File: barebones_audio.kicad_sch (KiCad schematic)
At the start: 40 parts, among them U10 ES8316, U30 TS3A227EYFFR, U31 STM32H743VIH6, U38 TPA2012D2RTJT

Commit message: Fixed version control merge issues
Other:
- note added: "ADC + DAC"
- note removed: "AUTOMATIC AUDIO DET"
- note removed: "Error: Cannot add L1 (footprint 'XAL7030-472MEB:IND_XAL7030-472MEB' not found). Error: Cannot update L2 (footprint 'XAL7030-472MEB:IND_XAL7030-472MEB' not found). Error: Cannot add U30 (footprint 'TS3A227EYFFR:BGA16N40P4X4_175X175X62N' not found). Error: Cannot add U27 (footprint 'IHLP1616ABERR47M01:IHLP-ER2' not found). Error: Cannot add L10 (footprint 'XAL7030-472MEB:IND_XAL7030-472MEB' not fou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"
- note removed: "LOW POWER AUDIO CODEC"
- moved on the sheet: C195, C196, C197, C198, C199, C200, C201, C202, C203, C204, R109, S1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

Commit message: Day 8 updated files
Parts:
- added C223: 0.1uF, Capacitor_SMD:C_0603_1608Metric, symbol Device:C
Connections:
- net AGND: now also C223.2
- net at S1.1: now also C223.1
- net PWR_BUTTON: now reaches S1.3
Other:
- moved on the sheet: MK1, S1

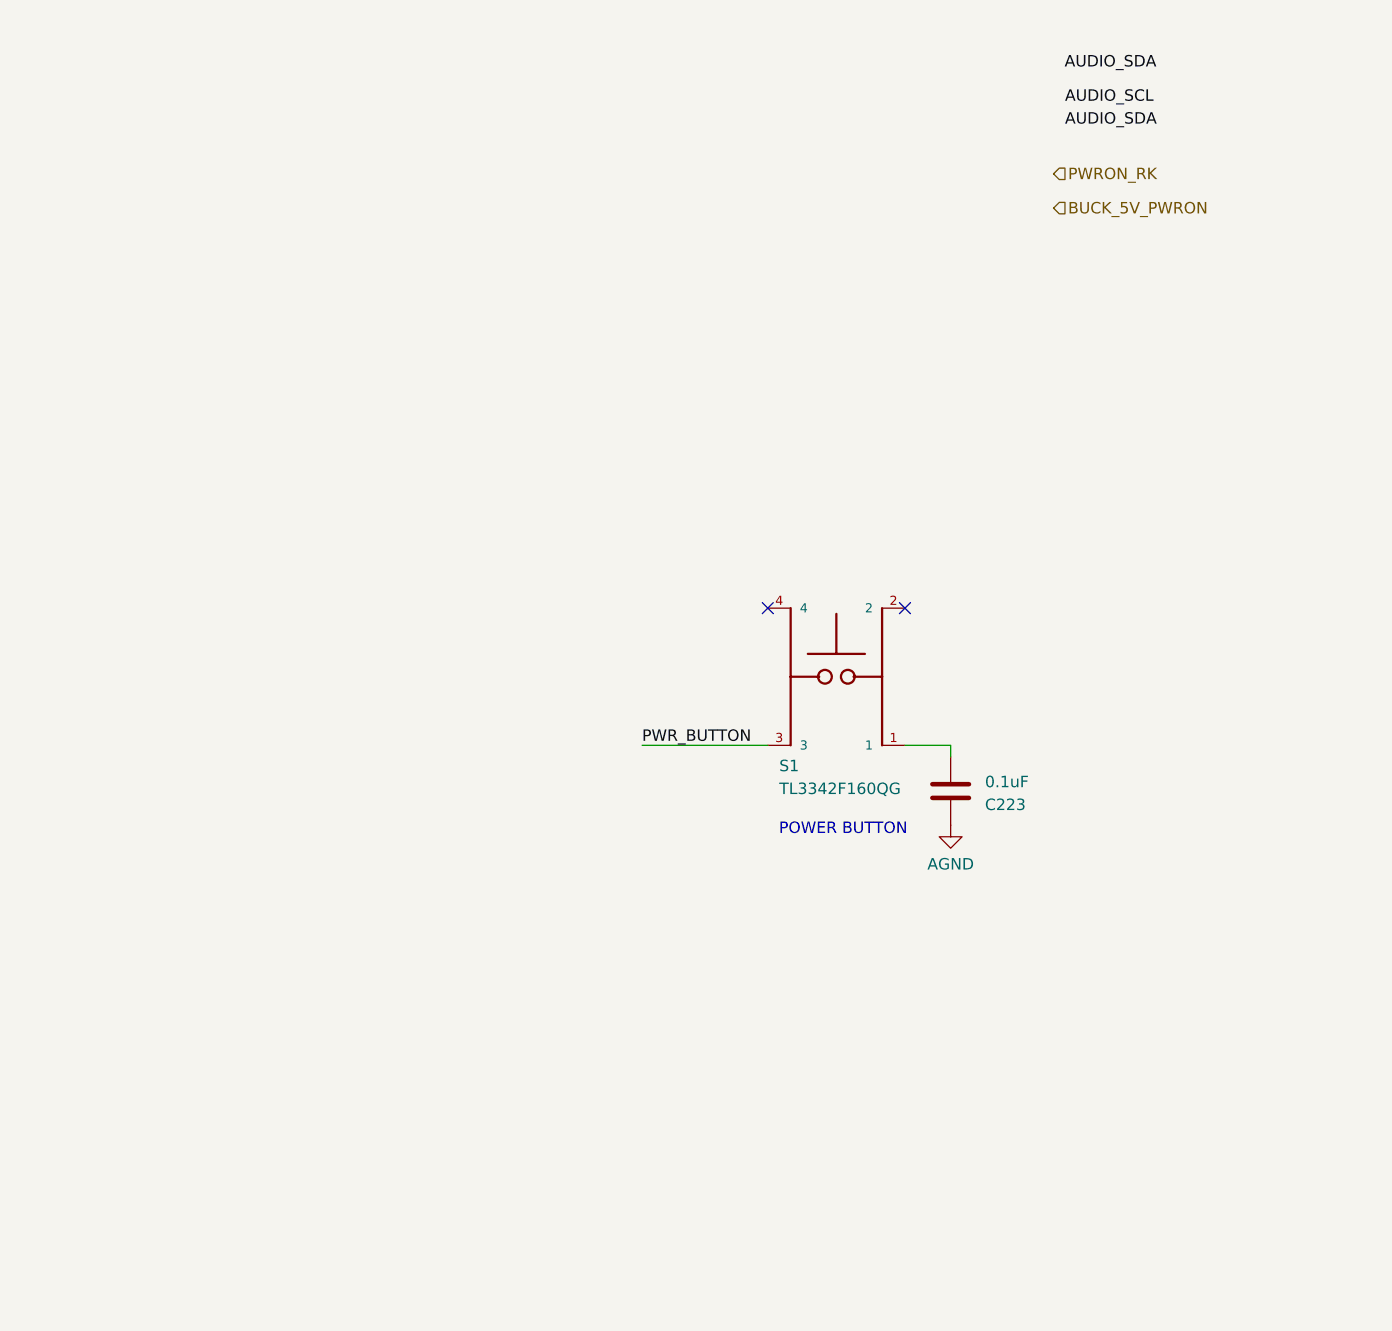
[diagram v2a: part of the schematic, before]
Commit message: fixed the power distribution by adding RK806 chips
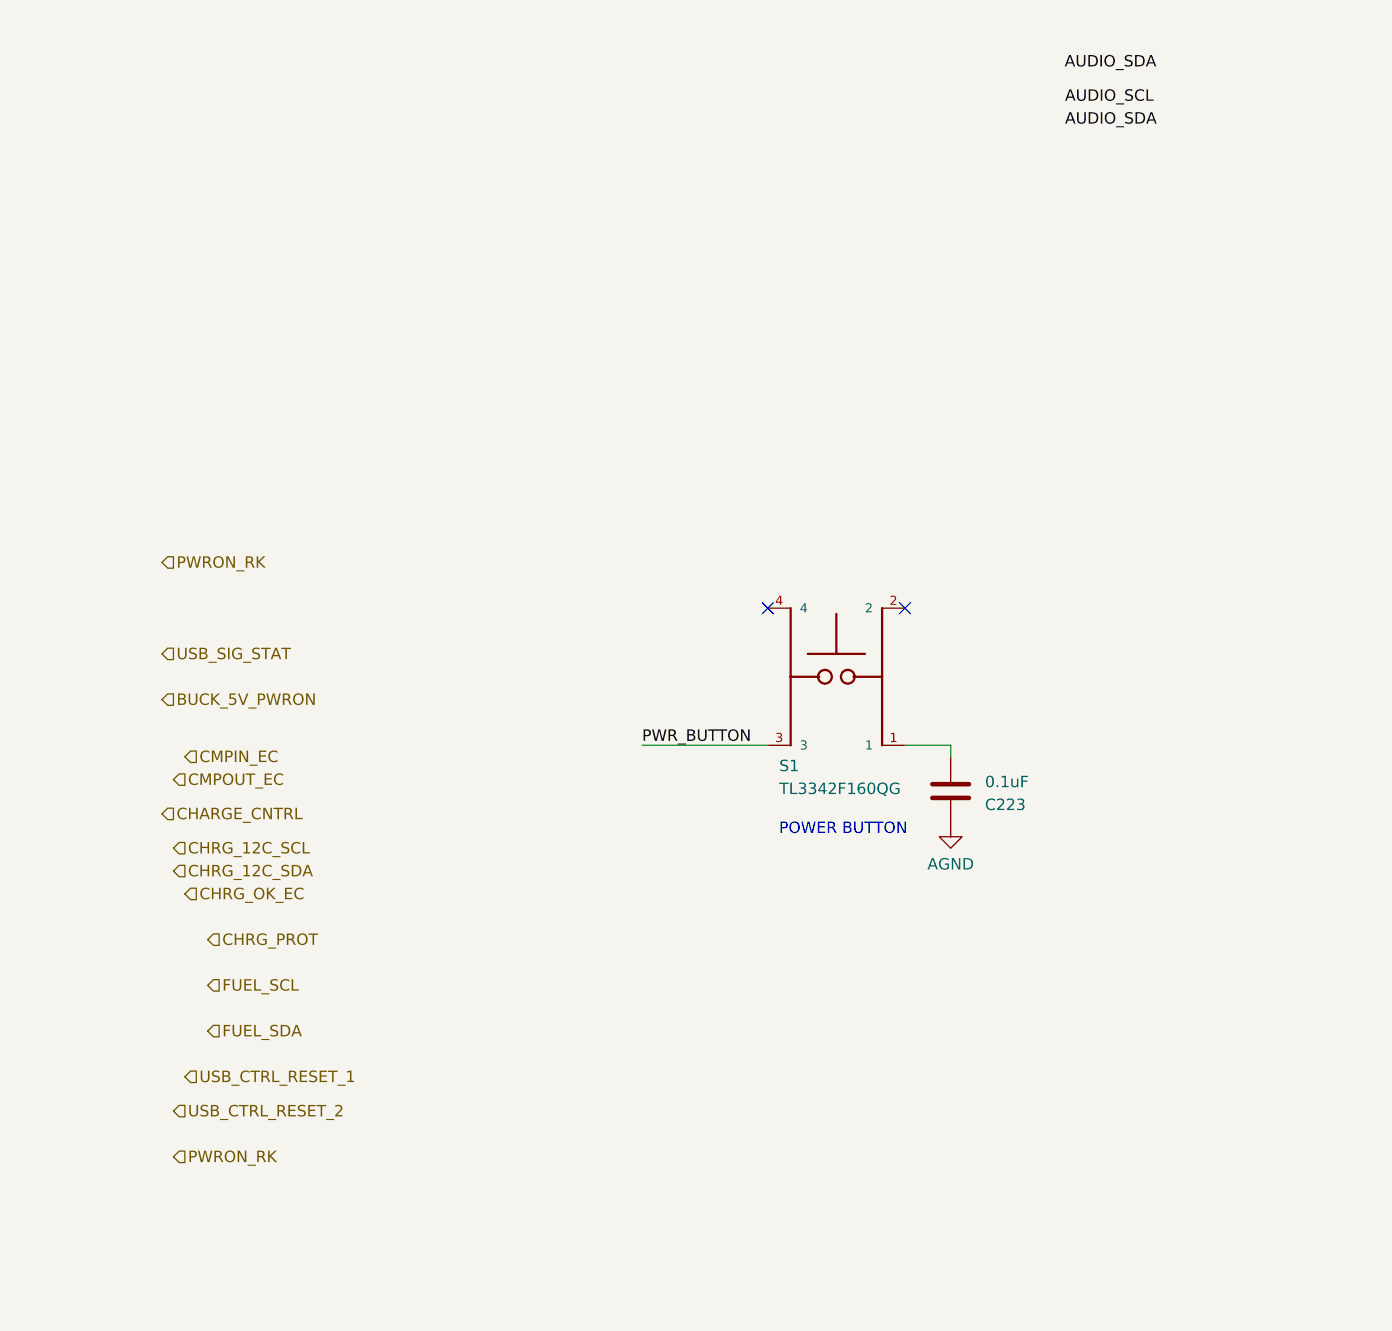
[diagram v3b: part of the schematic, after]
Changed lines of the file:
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@@
+		)
+	)
+	(hierarchical_label "CMPIN_EC"
+		(shape input)
+		(at 457.2 185.42 0)
+		(effects
+			(font
+				(size 1.27 1.27)
+			)
+			(justify left)
 		)
 	)
@@
 		)
 	)
+	(hierarchical_label "CHARGE_CNTRL"
+		(shape input)
+		(at 454.66 191.77 0)
+		(effects
+			(font
+				(size 1.27 1.27)
+			)
+			(justify left)
+		)
+	)
+	(hierarchical_label "CHRG_PROT"
+		(shape input)
+		(at 459.74 205.74 0)
+		(effects
+			(font
+				(size 1.27 1.27)
+			)
+			(justify left)
+		)
+	)
 	(hierarchical_label "JACK_SLEEVE"
 		(shape input)
@@
 		)
 	)
+	(hierarchical_label "CHRG_OK_EC"
+		(shape input)
+		(at 457.2 200.66 0)
+		(effects
+			(font
+				(size 1.27 1.27)
+			)
+			(justify left)
+		)
+	)
 	(hierarchical_label "AMP_MUTE"
 		(shape input)
@@
 	(hierarchical_label "PWRON_RK"
 		(shape input)
-		(at 553.72 120.65 0)
+		(at 454.66 163.83 0)
 		(effects
 			(font
@@
 		)
 	)
+	(hierarchical_label "CHRG_12C_SCL"
+		(shape input)
+		(at 455.93 195.58 0)
+		(effects
+			(font
+				(size 1.27 1.27)
+			)
+			(justify left)
+		)
+	)
+	(hierarchical_label "BUCK_5V_PWRON"
+		(shape input)
+		(at 454.66 179.07 0)
+		(effects
+			(font
+				(size 1.27 1.27)
+			)
+			(justify left)
+		)
+	)
 	(hierarchical_label "JACK_RING_2"
 		(shape input)
@@
 		)
 	)
+	(hierarchical_label "USB_CTRL_RESET_2"
+		(shape input)
+		(at 455.93 224.79 0)
+		(effects
+			(font
+				(size 1.27 1.27)
+			)
+			(justify left)
+		)
+	)
 	(hierarchical_label "ES_CCLK"
 		(shape input)
@@
 		)
 	)
+	(hierarchical_label "FUEL_SDA"
+		(shape input)
+		(at 459.74 215.9 0)
+		(effects
+			(font
+				(size 1.27 1.27)
+			)
+			(justify left)
+		)
+	)
+	(hierarchical_label "CMPOUT_EC"
+		(shape input)
+		(at 455.93 187.96 0)
+		(effects
+			(font
+				(size 1.27 1.27)
+			)
+			(justify left)
+		)
+	)
 	(hierarchical_label "SPK_OUT_R+"
 		(shape input)
@@
 		)
 	)
+	(hierarchical_label "USB_CTRL_RESET_1"
+		(shape input)
+		(at 457.2 220.98 0)
+		(effects
+			(font
+				(size 1.27 1.27)
+			)
+			(justify left)
+		)
+	)
 	(hierarchical_label "SPK_OUT_L-"
 		(shape input)
@@
 		)
 	)
+	(hierarchical_label "USB_SIG_STAT"
+		(shape input)
+		(at 454.66 173.99 0)
+		(effects
+			(font
+				(size 1.27 1.27)
+			)
+			(justify left)
+		)
+	)
+	(hierarchical_label "FUEL_SCL"
+		(shape input)
+		(at 459.74 210.82 0)
+		(effects
+			(font
+				(size 1.27 1.27)
+			)
+			(justify left)
+		)
+	)
 	(hierarchical_label "VCC_1V8_ES"
 		(shape input)
@@
 		)
 	)
-	(hierarchical_label "BUCK_5V_PWRON"
-		(shape input)
-		(at 553.72 124.46 0)
+	(hierarchical_label "PWRON_RK"
+		(shape input)
+		(at 455.93 229.87 0)
 		(effects
 			(font
@@
 		)
 	)
+	(hierarchical_label "CHRG_12C_SDA"
+		(shape input)
+		(at 455.93 198.12 0)
+		(effects
+			(font
+				(size 1.27 1.27)
+			)
+			(justify left)
+		)
+	)

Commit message: added the STM32L433RCT6 to act as the embedded controller
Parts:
- removed U31: STM32H743VIH6, barebones:BGA100C80P10X10_800X800X120, symbol STM32H743VIH6:STM32H743VIH6
- added C247, C248, C249, C250, C251, C252, C523: 100nF, Capacitor_SMD:C_0603_1608Metric, symbol Device:C
- added C253, C522: 20pF, Capacitor_SMD:C_0603_1608Metric, symbol Device:C
- added C521: 0.1uF, Capacitor_SMD:C_0603_1608Metric, symbol Device:C
- added C524: 1uF, Capacitor_SMD:C_0603_1608Metric, symbol Device:C
- added LED1: SK6812SIDE-A, easyeda2kicad:LED-SMD_4P-L4.0-W1.6-L, symbol SK6812_SIDE-A:SK6812SIDE-A_C5378721
- added R120: 2.2k, Resistor_SMD:R_0603_1608Metric, symbol Device:R
- added R121: 100k, Resistor_SMD:R_0603_1608Metric, symbol Device:R
- added R122: 1k, Resistor_SMD:R_0603_1608Metric, symbol Device:R
- added R123, R124: 10k, Resistor_SMD:R_0603_1608Metric, symbol Device:R
- added R125: 120R, Resistor_SMD:R_0603_1608Metric, symbol Device:R
- added R126, R127: 22R, Resistor_SMD:R_0603_1608Metric, symbol Device:R
- added R228: 2.2k, Resistor_SMD:R_0402_1005Metric, symbol Device:R
- added U48: STM32L433RCT6, easyeda2kicad:LQFP-64_L10.0-W10.0-P0.50-LS12.0-BL, symbol STM32L433RCT6:STM32L433RCT6
- added U67: PCA9306DCTR, barebones:SOP65P400X130-8N, symbol PCA9306DCTR:PCA9306DCTR
- added Y2: ABS07-32.768KHZ-T, ABS07-32.768KHZ-T:XTAL_ABS07-32.768KHZ-T, symbol ABS07-32.768KHZ-T:ABS07-32.768KHZ-T
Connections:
- net AGND: now also C247.2, C248.2, C249.2, C250.2, C251.2, C252.2, C253.2, C521.2, C522.2, C523.2, C524.2, LED1.4 (GND), R123.1, U48.12 (VSSA/VREF-), U48.18 (VSS), U48.31 (VSS), U48.47 (VSS), U48.63 (VSS), U67.1 (GND)
- net CHARGE_CNTRL: now also U48.17 (PA3)
- net CHRG_12C_SCL: now also U48.29 (PB10)
- net CHRG_12C_SDA: now also U48.30 (PB11)
- net CHRG_OK_EC: now also U48.15 (PA1)
- net CHRG_PROT: now also U48.16 (PA2)
- net FUEL_SCL: now also U48.58 (PB6)
- net FUEL_SDA: now also U48.59 (PB7)
- net PWRON_RK: now also U48.24 (PC4)
- net PWR_BUTTON: now also R122.1, U48.2 (PC13); no longer S1.3
- net USB_CTRL_RESET_1: now also U48.20 (PA4)
- net USB_CTRL_RESET_2: now also U48.21 (PA5)
- net USB_SIG_STAT: now also U48.22 (PA6)
- net VCC_3V3_ALW: now also C248.1, C249.1, C250.1, C251.1, C252.1, C524.1, R121.1, R124.1, R125.1, R228.1, U48.19 (VDD), U48.32 (VDD), U48.48 (VDDUSB), U48.64 (VDD)
- net at S1.4: now also R121.2
- new net: R127.2, U48.46 (PA13)
- new net: R126.2, U48.49 (PA14)
- new net: R123.2, U48.60 (PH3-BOOT0)
- new net: R122.2, S1.3
- new net: R228.2, U67.7 (VREF2)
- new net: LED1.1 (DIN), R120.2
- new net BUCK_PWRON: U48.25 (PC5)
- new net CMOS_PWR: C247.1, U48.1 (VBAT)
- new net I2C4_SCL_M1: U67.3 (SCL1)
- new net I2C4_SDA_M1: U67.4 (SDA1)
- new net I2C_SCL_CONN: U48.61 (PB8), U67.6 (SCL2)
- new net I2C_SDA_CONN: U48.62 (PB9), U67.5 (SDA2)
- new net LED_INDICATOR: R120.1
- new net NRST_7: C523.1, R124.2, U48.7 (NRST)
- new net OSC32_IN: C522.1, U48.3 (PC14-OSC32_IN), Y2.1
- new net OSC32_OUT: C253.1, U48.4 (PC15-OSC32_OUT), Y2.2
- new net RESETB_RK: U48.23 (PA7)
- new net SWCLK_14: R126.1
- new net SWDIO_13: R127.1
- new net SYS_WAKE: U48.57 (PB5)
- new net VCC_1V8_S0: U67.2 (VREF1), U67.8 (EN)
- new net VCC_5V0_ALW: C521.1, LED1.2 (VDD)
- new net VDDA_13: R125.2, U48.13 (VDDA/VREF+)
- no-connect marks 7 -> 37

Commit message: added the display connector and its 12V power supply
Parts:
- renumbered C194 to C394, C193 to C395, C186 to C396, C189 to C397, C187 to C398, C173 to C399, C166 to C400, C167 to C401, C172 to C402, C174 to C403, C188 to C404, C171 to C405, C169 to C406, C170 to C407, C223 to C408, C522 to C409, C253 to C410, C521 to C411, C199 to C412, C201 to C413, C200 to C414, C202 to C415, C247 to C416, C523 to C417, C195 to C418, C203 to C419, C196 to C420, C524 to C421, C248 to C422, C197 to C423, C204 to C424, C251 to C425, C198 to C426, C249 to C427, C252 to C428, C250 to C429, R104 to R126, R105 to R127, R108 to R128, R107 to R129, R102 to R130, R103 to R131, R106 to R132, R121 to R133, R122 to R134, R228 to R135, R120 to R136, R124 to R137, R123 to R138, R125 to R139, R126 to R140, R109 to R141, R127 to R142, U10 to U34, U30 to U35, U67 to U36, U38 to U37, U48 to U38
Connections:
- net KSI2: now reaches U38.10 (PC2)
- net KSI3: now reaches U38.11 (PC3)
- net SWO_14: now reaches U38.14 (PA0)
- net KSI4: now reaches U38.26 (PB0)
- net KSI5: now reaches U38.27 (PB1)
- net KSI6: now reaches U38.28 (PB2)
- net KSO0: now reaches U38.33 (PB12)
- net KSO1: now reaches U38.34 (PB13)
- net KSO2: now reaches U38.35 (PB14)
- net KSO3: now reaches U38.36 (PB15)
- net KSO4: now reaches U38.37 (PC6)
- net KSO5: now reaches U38.38 (PC7)
- net KSO6: now reaches U38.39 (PC8)
- net KSO7: now reaches U38.40 (PC9)
- net KSO8: now reaches U38.41 (PA8)
- net KSO9: now reaches U38.42 (PA9)
- net KSO10: now reaches U38.43 (PA10)
- net KSO11: now reaches U38.44 (PA11)
- net KSO12: now reaches U38.45 (PA12)
- net KSI7: now reaches U38.50 (PA15)
- net KSO13: now reaches U38.51 (PC10)
- net KSO14: now reaches U38.52 (PC11)
- net KSO15: now reaches U38.53 (PC12)
- net CAPS_P: now reaches U38.54 (PD2)
- net BACKLIGHT_PWM: now reaches U38.56 (PB4)
- net KSI0: now reaches U38.8 (PC0)
- net KSI1: now reaches U38.9 (PC1)
- net SWCLK_14 renamed SWCLK_49
- net SWDIO_13 renamed SWDIO_46
- no-connect marks 37 -> 9
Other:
- moved on the sheet: R138, R140

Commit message: added the PCF85063ATL/1,118 CMOS Real-Time Clock
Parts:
- removed C411: 0.1uF, Capacitor_SMD:C_0603_1608Metric, symbol Device:C
- removed LED1: SK6812SIDE-A, easyeda2kicad:LED-SMD_4P-L4.0-W1.6-L, symbol SK6812_SIDE-A:SK6812SIDE-A_C5378721
- removed R136: 2.2k, Resistor_SMD:R_0603_1608Metric, symbol Device:R
- added C523, C525: 10uF, Capacitor_SMD:C_0603_1608Metric, symbol Device:C
- C402: value 1uF -> 4.7uF
- C404: value 1uF -> 10uF
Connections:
- net AGND: now also C523.1, C525.1
- net RIN2: now reaches U34.27 (RIN2)
- net RIN2: now also C523.2
- net LIN2: now reaches U34.28 (LIN2)
- net LIN2: now also C525.2
- net CMOS_PWR renamed V_BAT_CMOS
- net I2C4_SCL_M1 renamed I2C1_SCL_M2
- net I2C4_SDA_M1 renamed I2C1_SDA_M2
- net R1N1 renamed RIN1
- net SYS_WAKE renamed HALL_SENSE
- no-connect marks 9 -> 6
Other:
- moved on the sheet: C396, U34, U35

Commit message: updated the Fuel Guage/BMS module for the 4S battery usage
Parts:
- removed C394, C395: 1uF, Capacitor_SMD:C_0603_1608Metric, symbol Device:C
- removed NT1, NT2: NetTie_2, NetTie:NetTie-2_SMD_Pad0.5mm, symbol Device:NetTie_2
- removed R126, R127: 33, Resistor_SMD:R_0603_1608Metric, symbol Device:R
- removed R128: 10k, Resistor_SMD:R_0603_1608Metric, symbol Device:R
- added C542: 1uF, Capacitor_SMD:C_0603_1608Metric, symbol Device:C
- added J22: SJ2-35894B-SMT-TR, barebones:CUI_SJ2-35894B-SMT-TR, symbol SJ2-35894B-SMT-TR:SJ2-35894B-SMT-TR
- added MK2: CMM-2718AT-3817NC-TR, CMM-2718AT-3817NC-TR:MIC_CMM-2718AT-3817NC-TR, symbol CMM-2718AT-3817NC-TR:CMM-2718AT-3817NC-TR
- added NT3, NT4: NetTie_2, NetTie:NetTie-2_SMD_Pad0.5mm, symbol Device:NetTie_2
- added R216, R217, R218: 4.7k, Resistor_SMD:R_0603_1608Metric, symbol Device:R
- added R219: 10k, Resistor_SMD:R_0603_1608Metric, symbol Device:R
- C396, C398: value 1uF -> 10uF
- C397, C399, C405, C406, C407: value 1uF -> 100nF
- C400, C401: value 0.1uF -> 10uF
- C402: value 4.7uF -> 10uF
- C403: value 1uF -> 4.7uF
- MK1: footprint SPH0645LM4H-B:MIC_SPH0645LM4H-B -> barebones:MIC_SPH0645LM4H-B
- R129: value 2.2k -> 330k
- R130: value 2.2k -> 10k
- R132: value 2.2k -> 4.7k
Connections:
- net ES_GPIO3 is gone; now on net HP_INT: U34.12 (GPIO3)
- net ADCVREF: now also C402.2; no longer C405.2
- net AGND: no longer C397.1, C399.1, C400.1, C401.1, C402.1, C403.1, C404.2, C405.1, C406.1, C407.1, C408.2, C409.2, C410.2, C412.2, C413.2, C414.2, C415.2, C416.2, C417.2, C419.2, C420.2, C421.2, C422.2, C424.2, C425.2, C426.2, C427.2, C428.2, C429.2, C523.1, C525.1, R138.1, U34.31 (CE), U35.A2 (GND), U35.B2 (GND), U35.D2 (GNDA), U36.1 (GND), U37.1 (G1), U37.12 (PGND), U37.18 (AGND), U37.21 (EXP), U37.4 (PGND), U38.12 (VSSA/VREF-), U38.18 (VSS), U38.31 (VSS), U38.47 (VSS), U38.63 (VSS)
- net CPVSSP: now also C399.1, C400.1; no longer C406.2
- net DACVREF: now also C401.2; no longer C407.2
- net GNDREF: no longer U35.A4 (GND_SENSE)
- net LIN1: now also C542.2
- net LIN2: now also C405.2; no longer C525.2
- net MICBIAS: now also C404.2, R131.1; no longer C404.1, R129.2, R132.1
- net PVDD: now also C523.1; no longer C400.2, C401.2, C403.2, U34.14 (CPVDD), U34.3 (DVDD), U34.4 (PVDD), U37.15 (G0)
- net RIN2: now also C406.2; no longer C523.2
- net VCC_1V8_S0: now also C397.1, C398.1, R129.1, R130.1, U34.3 (DVDD), U34.4 (PVDD), NT3.1
- net VMID: now also C403.2; no longer C402.2
- net MIC_PRESENT: now reaches U35.A1 (~{MIC_PRESENT})
- net MIC_PRESENT: now also R217.2
- net AMP_MUTE renamed SPK_MUTE
- net AUDIO_SCL renamed SCL_AUDIO
- net SCL_AUDIO: now also R132.2
- net AUDIO_SDA renamed INT_AUDIO
- net INT_AUDIO: now also R216.2; no longer U35.B3 (SDA)
- net CODEC_MIC renamed HP_MICP
- net HP_MICP: now also R131.2, C542.1; no longer R129.1
- net ES_ASDOUT renamed I2S0_SDI0
- net ES_CCLK renamed HP_INT
- net HP_INT: no longer U34.1 (CCLK)
- net ES_CDATA renamed I2C7_SDA_M0
- net I2C7_SDA_M0: no longer R131.2
- net ES_DSIN renamed I2S0_SDO0
- net ES_LRCK renamed I2S0_LRCK_TX
- net ES_MCLK renamed I2S0_MLCK
- net ES_SCLK renamed I2S0_SCLK_TX
- net JACK_MIC_1 renamed GND
- net GND: now also C397.2, C399.2, C400.2, C401.1, C402.1, C403.1, C404.1, C405.1, C406.1, C407.2, C408.2, C409.2, C410.2, C412.2, C413.2, C414.2, C415.2, C416.2, C417.2, C419.2, C420.2, C421.2, C422.2, C424.2, C425.2, C426.2, C427.2, C428.2, C429.2, C523.2, C525.2, R138.1, U35.A2 (GND), U35.A4 (GND_SENSE), U35.B2 (GND), U35.D2 (GNDA), U36.1 (GND), U37.1 (G1), U37.12 (PGND), U37.15 (G0), U37.18 (AGND), U37.21 (EXP), U37.4 (PGND), U38.12 (VSSA/VREF-), U38.18 (VSS), U38.31 (VSS), U38.47 (VSS), U38.63 (VSS), MK2.3 (GND), MK2.4 (GND)
- net JACK_RING_2 renamed HP_JACK_RING_2
- net HP_JACK_RING_2: now also J22.4
- net JACK_SLEEVE renamed HP_JACK_SLEEVE
- net HP_JACK_SLEEVE: now also J22.1; no longer C398.1, R132.2
- net JACK_SWITCH renamed HP_DET_TRIGGER
- net HP_DET_TRIGGER: now also J22.10
- net JACK_TIP renamed HP_JACK_TIP
- net HP_JACK_TIP: now also J22.2
- net RIN1: no longer names the net of U34.29 (RIN1)
- removed net VCC_1V8_SYS: R130.1, R131.1
- removed net VCC_3V3_SYS: C397.2, C399.2, U34.22 (AVDD), U35.A3 (VDD)
- new net AVDD: U34.22 (AVDD)
- new net CPVDD: NT3.2, NT4.1, U34.14 (CPVDD)
- new net ES_CE: R219.1, U34.31 (CE)
- new net HP_DETECT: R129.2
- new net I2C7_SCL_M0: U34.1 (CCLK)
- new net SDA_AUDIO: R218.2, U35.B3 (SDA)
- new net VCC_3V3_S3: C407.1, C525.1, R132.1, R216.1, R217.1, R218.1, U35.A3 (VDD)
- new net VCC_ES_CE: NT4.2, R219.2
- no-connect marks 6 -> 7
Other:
- note added: "AUDIO CODEC"
- note removed: "ADC + DAC"
- moved on the sheet: C396, C409, C410, C412, C413, C414, C415, C416, C417, C418, C419, C420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
